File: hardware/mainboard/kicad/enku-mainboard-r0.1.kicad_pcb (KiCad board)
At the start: 4 copper layers, 54 x 94 mm, 122 parts, among them J1 1S LiPo + NTC, J2 Hirose DM3AT-SF-PEJM5, J3 FH34SRJ-24S-0.5SH(50), J5 GCT USB4105-GF-A-120, J6 4-pin pogo dock, J7 Tag-Connect TC2030-IDC-NL, Q1 IRLML6346TRPBF, SW1 HARD POWER, SW2 BOOT / RECOVERY, SW3 BTN_L1, SW4 BTN_L2, SW5 BTN_R1, SW6 BTN_R2, U1 ESP32-S3-WROOM-1-N16R8, U2 TPS2121, U3 BQ25185DLHR, U4 TPS63802DLAR, U5 BMI270, U6 DRV5032FBDBZR, U8 USBLC6-2SC6

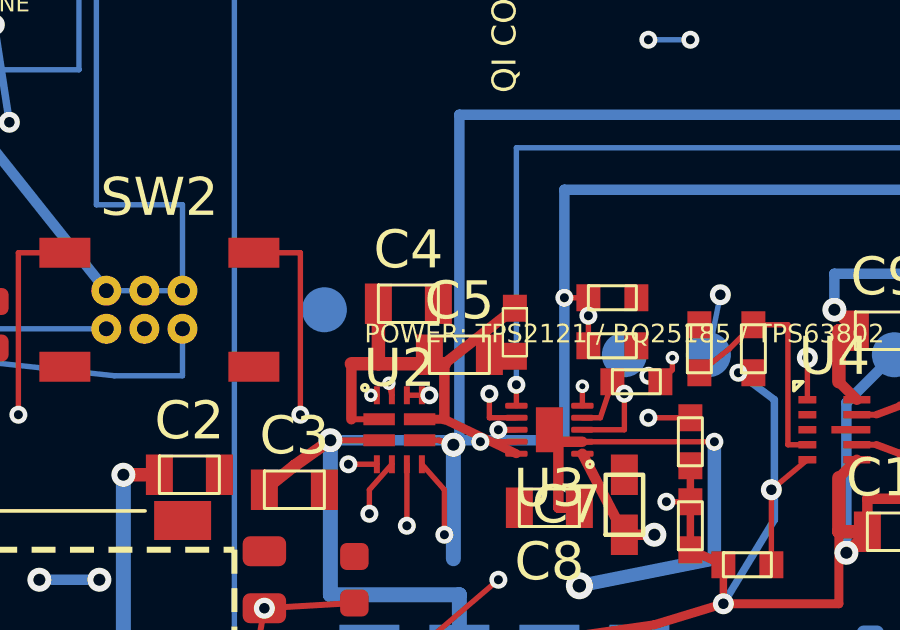
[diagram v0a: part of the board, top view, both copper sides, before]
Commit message: pcb: hop dock feed around USB corridor
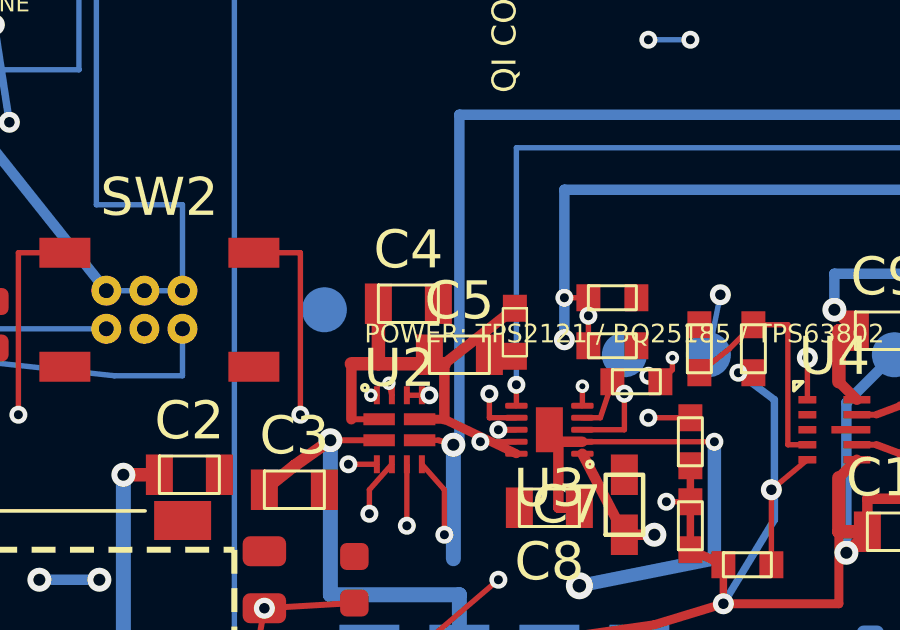
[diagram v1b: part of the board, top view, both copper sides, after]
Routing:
- net VBUS_DOCK: vias 2 -> 3
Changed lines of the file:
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@@
   (via (at 66.000 83.000) (size 0.70) (drill 0.35) (layers "F.Cu" "B.Cu") (net 79))
   (segment (start 66.000 83.000) (end 49.000 83.000) (width 0.35) (layer "B.Cu") (net 79))
-  (segment (start 49.000 83.000) (end 49.000 91.350) (width 0.35) (layer "B.Cu") (net 79))
-  (segment (start 49.000 91.350) (end 41.200 91.350) (width 0.35) (layer "B.Cu") (net 79))
   (segment (start 28.000 65.000) (end 29.000 65.000) (width 0.18) (layer "F.Cu") (net 23))
   (segment (start 29.000 65.000) (end 55.000 65.000) (width 0.18) (layer "F.Cu") (net 23))
@@
   (segment (start 32.000 70.000) (end 32.000 44.000) (width 0.18) (layer "B.Cu") (net 18))
   (segment (start 32.000 44.000) (end 42.500 44.000) (width 0.18) (layer "B.Cu") (net 18))
+  (segment (start 49.000 83.000) (end 49.000 88.000) (width 0.35) (layer "B.Cu") (net 79))
+  (via (at 49.000 88.000) (size 0.70) (drill 0.35) (layers "F.Cu" "B.Cu") (net 79))
+  (segment (start 49.000 88.000) (end 49.000 91.000) (width 0.35) (layer "In2.Cu") (net 79))
+  (segment (start 49.000 91.000) (end 41.200 91.000) (width 0.35) (layer "In2.Cu") (net 79))
+  (segment (start 41.200 91.000) (end 41.200 91.350) (width 0.35) (layer "In2.Cu") (net 79))
 )

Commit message: pcb: restore lower-DRC dock baseline
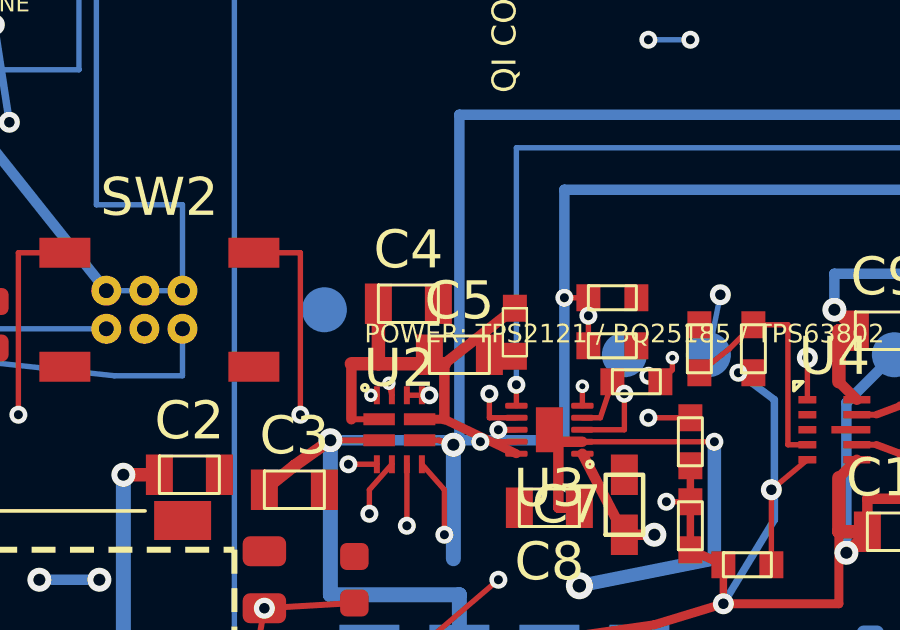
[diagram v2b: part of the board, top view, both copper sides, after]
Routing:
- net VBUS_DOCK: vias 3 -> 2
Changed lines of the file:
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@@
   (via (at 66.000 83.000) (size 0.70) (drill 0.35) (layers "F.Cu" "B.Cu") (net 79))
   (segment (start 66.000 83.000) (end 49.000 83.000) (width 0.35) (layer "B.Cu") (net 79))
+  (segment (start 49.000 83.000) (end 49.000 91.350) (width 0.35) (layer "B.Cu") (net 79))
+  (segment (start 49.000 91.350) (end 41.200 91.350) (width 0.35) (layer "B.Cu") (net 79))
   (segment (start 28.000 65.000) (end 29.000 65.000) (width 0.18) (layer "F.Cu") (net 23))
   (segment (start 29.000 65.000) (end 55.000 65.000) (width 0.18) (layer "F.Cu") (net 23))
@@
   (segment (start 32.000 70.000) (end 32.000 44.000) (width 0.18) (layer "B.Cu") (net 18))
   (segment (start 32.000 44.000) (end 42.500 44.000) (width 0.18) (layer "B.Cu") (net 18))
-  (segment (start 49.000 83.000) (end 49.000 88.000) (width 0.35) (layer "B.Cu") (net 79))
-  (via (at 49.000 88.000) (size 0.70) (drill 0.35) (layers "F.Cu" "B.Cu") (net 79))
-  (segment (start 49.000 88.000) (end 49.000 91.000) (width 0.35) (layer "In2.Cu") (net 79))
-  (segment (start 49.000 91.000) (end 41.200 91.000) (width 0.35) (layer "In2.Cu") (net 79))
-  (segment (start 41.200 91.000) (end 41.200 91.350) (width 0.35) (layer "In2.Cu") (net 79))
 )

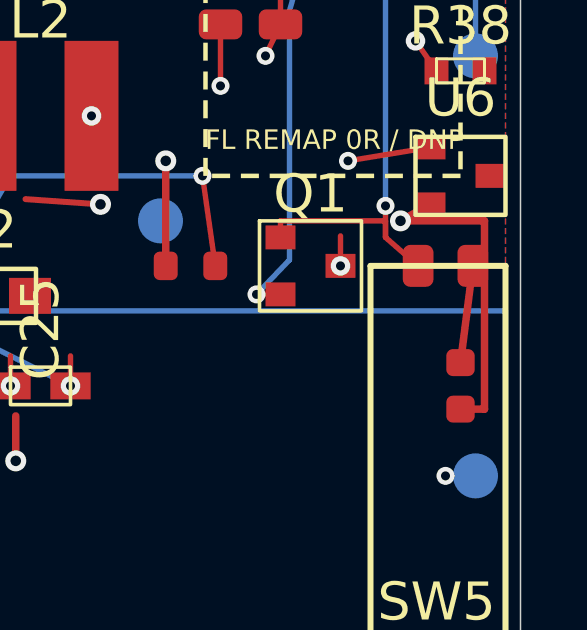
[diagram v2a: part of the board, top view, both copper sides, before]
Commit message: pcb: clear 3V3 route from R37 ground pad
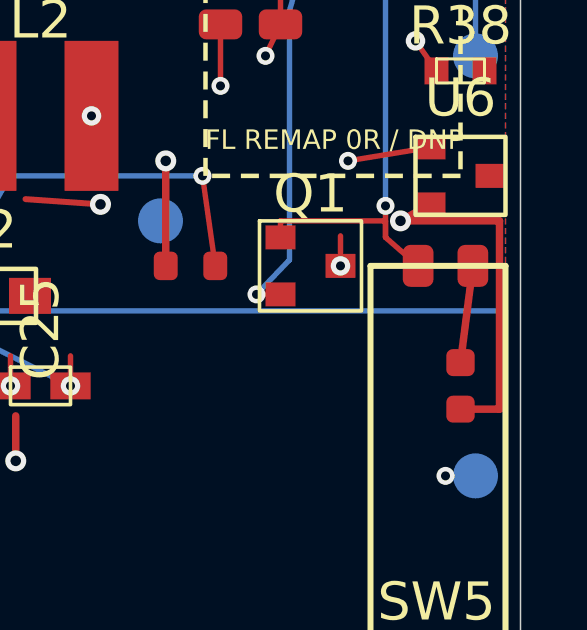
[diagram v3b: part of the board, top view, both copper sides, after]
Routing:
- net 3V3_SYS: track 290.4 -> 291.4 mm
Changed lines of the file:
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@@
   (segment (start 62.175 44.500) (end 57.175 54.500) (width 0.25) (layer "In2.Cu") (net 2))
   (segment (start 71.000 45.950) (end 70.000 46.500) (width 0.25) (layer "F.Cu") (net 2))
-  (segment (start 72.000 52.775) (end 72.800 52.775) (width 0.25) (layer "F.Cu") (net 2))
-  (segment (start 72.800 52.775) (end 72.800 46.500) (width 0.25) (layer "F.Cu") (net 2))
-  (segment (start 72.800 46.500) (end 70.000 46.500) (width 0.25) (layer "F.Cu") (net 2))
+  (segment (start 72.000 52.775) (end 73.300 52.775) (width 0.25) (layer "F.Cu") (net 2))
+  (segment (start 73.300 52.775) (end 73.300 46.500) (width 0.25) (layer "F.Cu") (net 2))
+  (segment (start 73.300 46.500) (end 70.000 46.500) (width 0.25) (layer "F.Cu") (net 2))
   (via (at 70.000 46.500) (size 0.70) (drill 0.35) (layers "F.Cu" "In2.Cu") (net 2))
   (segment (start 70.000 46.500) (end 62.175 44.500) (width 0.25) (layer "In2.Cu") (net 2))

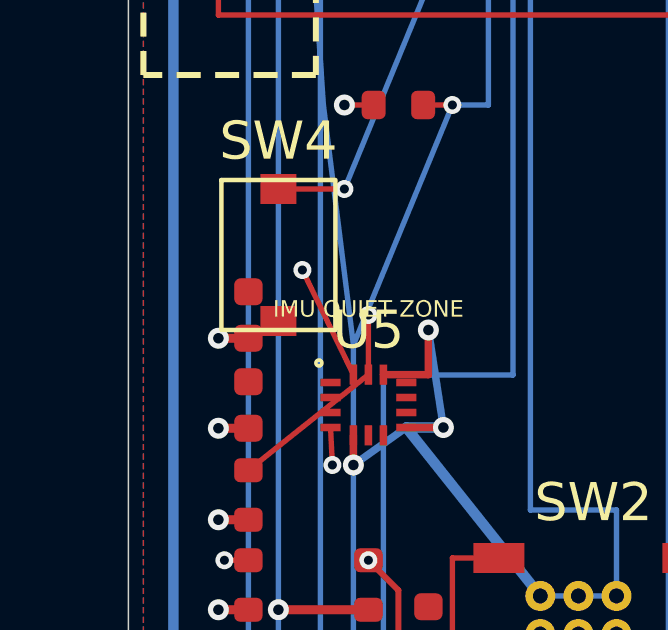
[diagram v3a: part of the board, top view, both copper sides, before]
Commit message: pcb: move C18 clear of left reading button
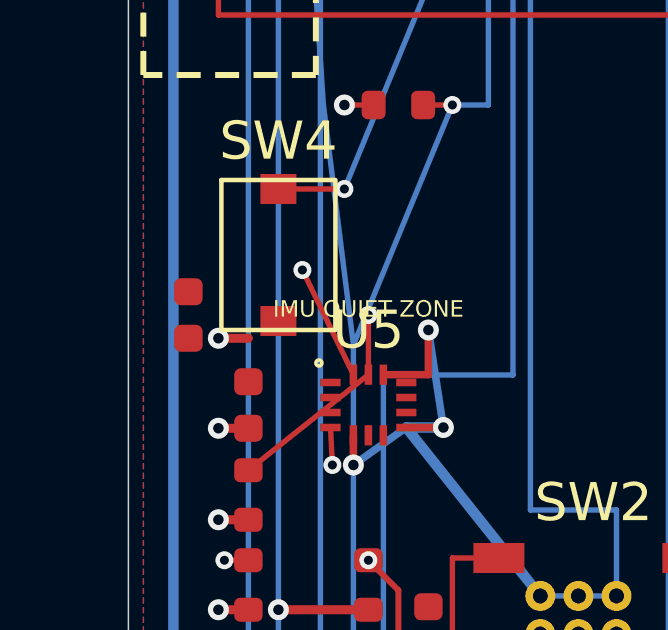
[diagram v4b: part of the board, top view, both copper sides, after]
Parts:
- moved C18 2.00 mm to (22.0, 77.0)
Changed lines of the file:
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@@
   )
   (footprint "Capacitor_SMD:C_0603_1608Metric" (layer "F.Cu")
-    (at 24 77 90)
+    (at 22 77 90)
     (property "Reference" "C18" (at 0 -1.5 90) (layer "F.SilkS") hide)
     (property "Value" "100nF" (at 0 1.5 90) (layer "F.Fab") hide)

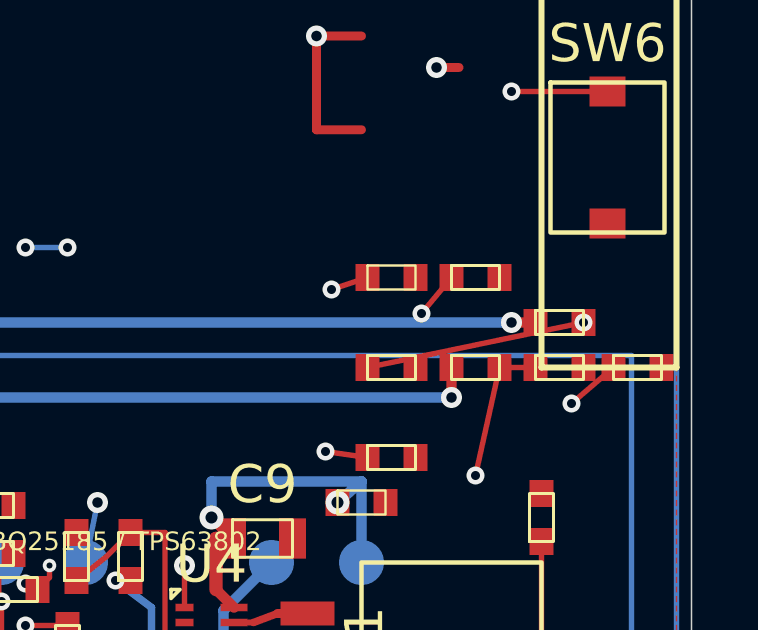
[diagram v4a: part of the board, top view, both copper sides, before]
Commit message: pcb: route MUX_PR1 around strap row pads
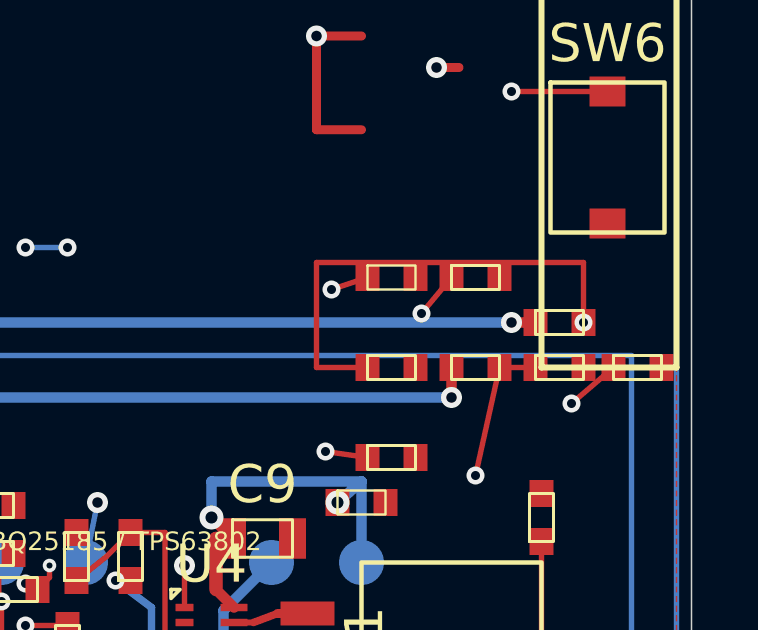
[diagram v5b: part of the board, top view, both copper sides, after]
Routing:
- net MUX_PR1: track 57.3 -> 66.1 mm
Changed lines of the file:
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@@
   (segment (start 70.40 76.80) (end 70.40 80.50) (width 0.18) (layer "In2.Cu") (net 82))
   (via (at 70.40 80.50) (size 0.60) (drill 0.30) (layers "F.Cu" "In2.Cu") (net 82))
-  (segment (start 70.40 80.50) (end 63.20 82.00) (width 0.18) (layer "F.Cu") (net 82))
+  (segment (start 70.40 80.50) (end 70.40 78.50) (width 0.18) (layer "F.Cu") (net 82))
+  (segment (start 70.40 78.50) (end 61.50 78.50) (width 0.18) (layer "F.Cu") (net 82))
+  (segment (start 61.50 78.50) (end 61.50 82.00) (width 0.18) (layer "F.Cu") (net 82))
+  (segment (start 61.50 82.00) (end 63.20 82.00) (width 0.18) (layer "F.Cu") (net 82))
   (segment (start 43.75 89.85) (end 44.50 89.85) (width 0.18) (layer "F.Cu") (net 87))
   (via (at 44.50 89.85) (size 0.60) (drill 0.30) (layers "F.Cu" "In2.Cu") (net 87))

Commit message: pcb: restore best baseline after MUX strap experiment
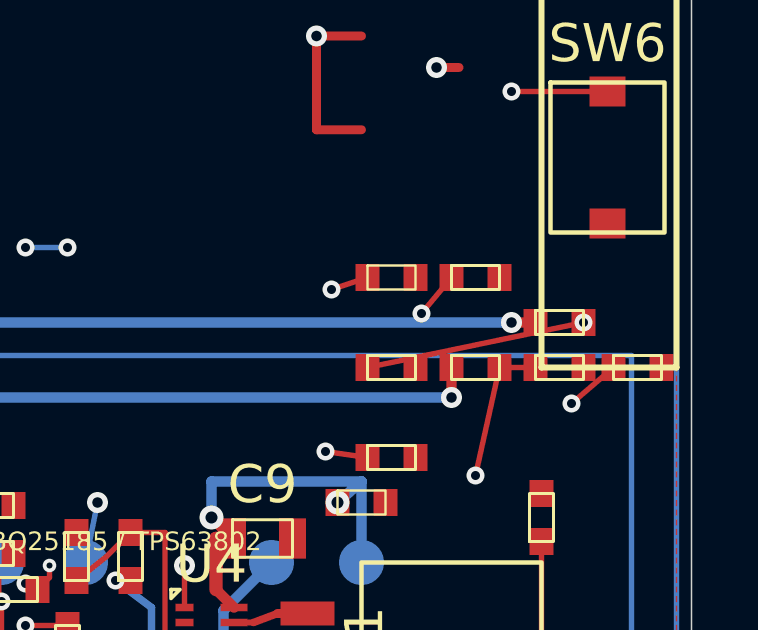
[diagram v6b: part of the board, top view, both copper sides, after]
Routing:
- net MUX_PR1: track 66.1 -> 57.3 mm
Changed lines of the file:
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@@
   (segment (start 70.40 76.80) (end 70.40 80.50) (width 0.18) (layer "In2.Cu") (net 82))
   (via (at 70.40 80.50) (size 0.60) (drill 0.30) (layers "F.Cu" "In2.Cu") (net 82))
-  (segment (start 70.40 80.50) (end 70.40 78.50) (width 0.18) (layer "F.Cu") (net 82))
-  (segment (start 70.40 78.50) (end 61.50 78.50) (width 0.18) (layer "F.Cu") (net 82))
-  (segment (start 61.50 78.50) (end 61.50 82.00) (width 0.18) (layer "F.Cu") (net 82))
-  (segment (start 61.50 82.00) (end 63.20 82.00) (width 0.18) (layer "F.Cu") (net 82))
+  (segment (start 70.40 80.50) (end 63.20 82.00) (width 0.18) (layer "F.Cu") (net 82))
   (segment (start 43.75 89.85) (end 44.50 89.85) (width 0.18) (layer "F.Cu") (net 87))
   (via (at 44.50 89.85) (size 0.60) (drill 0.30) (layers "F.Cu" "In2.Cu") (net 87))

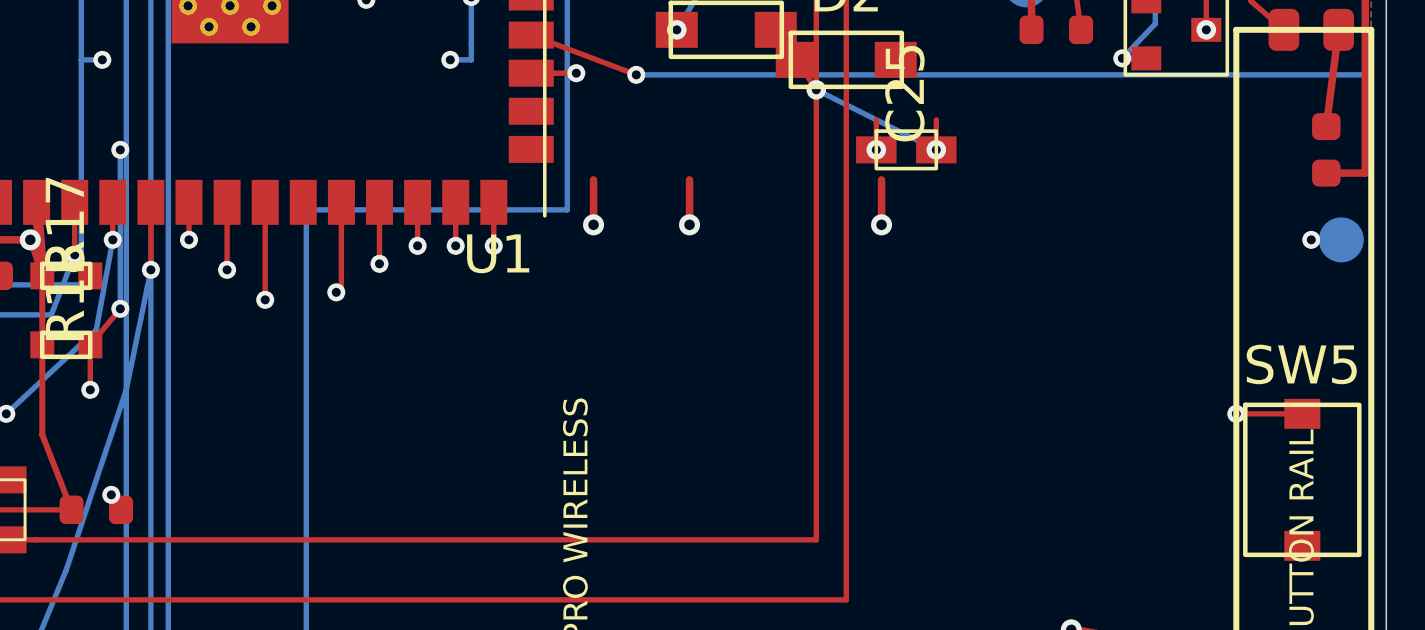
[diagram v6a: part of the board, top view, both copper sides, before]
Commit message: pcb: move BTN_R1 trunk off congested In2 layer
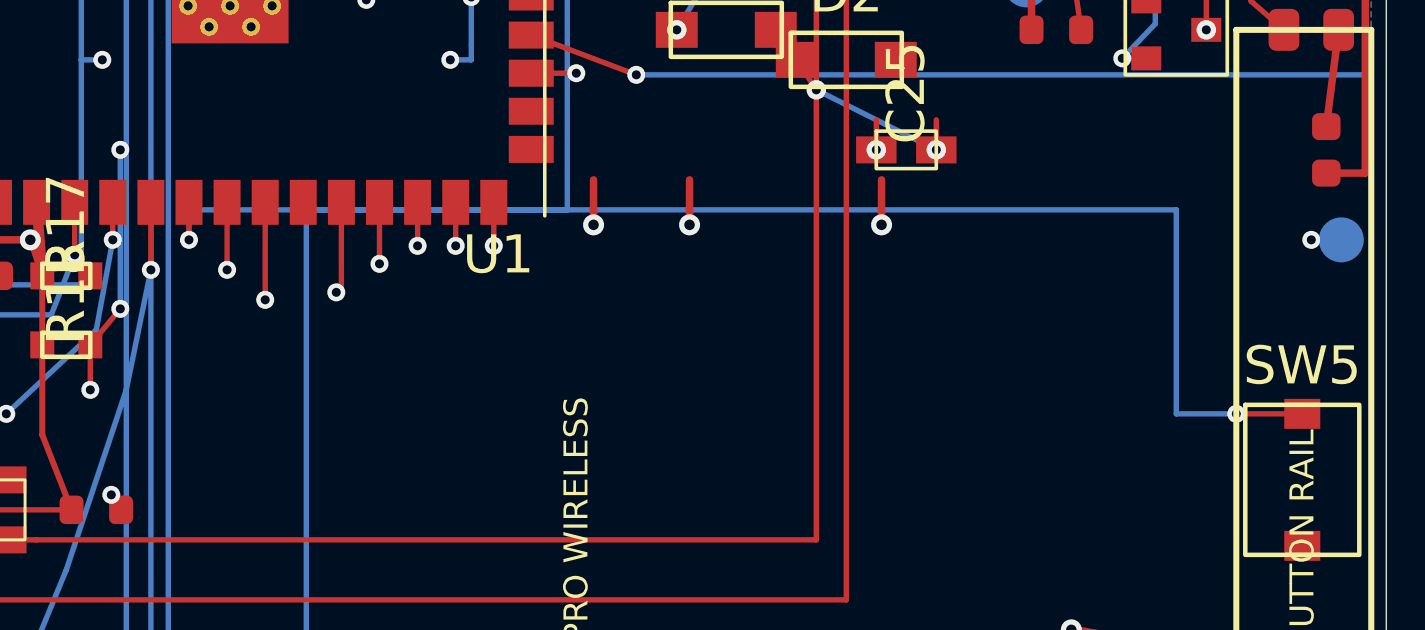
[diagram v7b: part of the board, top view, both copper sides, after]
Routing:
- net BTN_R1: track 44.2 -> 46.2 mm
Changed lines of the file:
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@@
   (segment (start 27.20 72.80) (end 25.00 72.80) (width 0.18) (layer "F.Cu") (net 49))
   (segment (start 34.09 53.75) (end 34.09 55.00) (width 0.18) (layer "F.Cu") (net 50))
-  (via (at 34.09 55.00) (size 0.60) (drill 0.30) (layers "F.Cu" "In2.Cu") (net 50))
-  (via (at 69.00 60.80) (size 0.60) (drill 0.30) (layers "F.Cu" "In2.Cu") (net 50))
+  (via (at 34.09 55.00) (size 0.60) (drill 0.30) (layers "F.Cu" "B.Cu") (net 50))
+  (via (at 69.00 60.80) (size 0.60) (drill 0.30) (layers "F.Cu" "B.Cu") (net 50))
   (segment (start 69.00 60.80) (end 71.20 60.80) (width 0.18) (layer "F.Cu") (net 50))
   (segment (start 35.36 53.75) (end 35.36 56.00) (width 0.18) (layer "F.Cu") (net 51))
@@
   (segment (start 34.000 89.200) (end 36.270 89.200) (width 0.18) (layer "B.Cu") (net 47))
   (segment (start 36.270 89.200) (end 36.270 87.635) (width 0.18) (layer "B.Cu") (net 47))
-  (segment (start 34.09 55.00) (end 67.00 55.00) (width 0.18) (layer "In2.Cu") (net 50))
-  (segment (start 67.00 55.00) (end 67.00 60.80) (width 0.18) (layer "In2.Cu") (net 50))
-  (segment (start 67.00 60.80) (end 69.00 60.80) (width 0.18) (layer "In2.Cu") (net 50))
   (segment (start 66.20 56.00) (end 66.20 72.80) (width 0.18) (layer "In2.Cu") (net 51))
   (segment (start 29.010 34.000) (end 22.000 50.000) (width 0.18) (layer "In2.Cu") (net 73))
@@
   (segment (start 32.000 70.000) (end 32.000 44.000) (width 0.18) (layer "B.Cu") (net 18))
   (segment (start 32.000 44.000) (end 42.500 44.000) (width 0.18) (layer "B.Cu") (net 18))
+  (segment (start 34.09 55.00) (end 34.09 54.00) (width 0.18) (layer "B.Cu") (net 50))
+  (segment (start 34.09 54.00) (end 67.00 54.00) (width 0.18) (layer "B.Cu") (net 50))
+  (segment (start 67.00 54.00) (end 67.00 60.80) (width 0.18) (layer "B.Cu") (net 50))
+  (segment (start 67.00 60.80) (end 69.00 60.80) (width 0.18) (layer "B.Cu") (net 50))
 )
